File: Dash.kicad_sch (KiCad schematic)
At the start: 89 parts, among them J1 Conn_01x03_Socket, J10 Conn_01x03_Socket, J11 Conn_01x04_Socket, J2 Conn_01x03_Socket, J3 Conn_01x03_Socket, J4 Conn_01x03_Socket, J5 Conn_01x03_Socket, J6 Conn_01x03_Socket, J7 Conn_01x07_Socket, J8 Conn_01x06_Socket, J9 Conn_01x05_Socket, Q1 2N7000, Q16 NMOS, Q17 NMOS, Q18 NMOS, Q19 NMOS, Q2 NMOS, Q20 NMOS, Q4 NMOS, Q5 NMOS, SW1 SW_Push, U1 SFH617A-1, U2 24C02Cx-x-SN, U3 24C02Cx-x-SN, U4 LM2678T-3.3, U5 LM2678T-5.0, U6 ESP32-S2-DevKitM

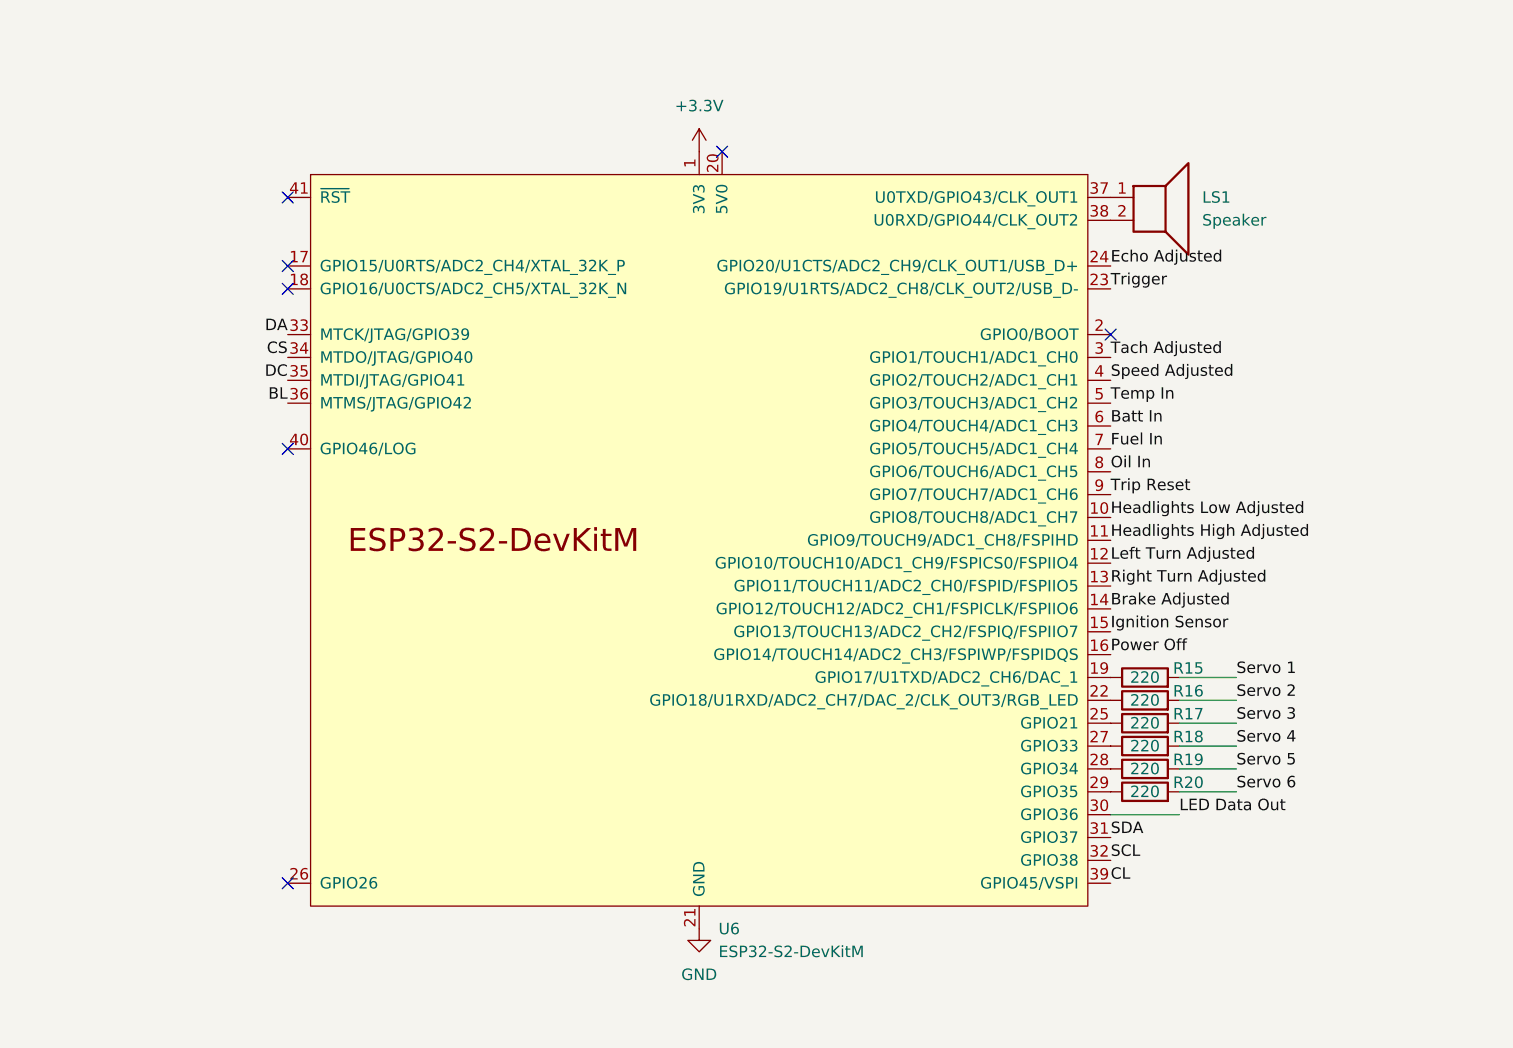
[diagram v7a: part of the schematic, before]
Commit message: Fixed pin assignments
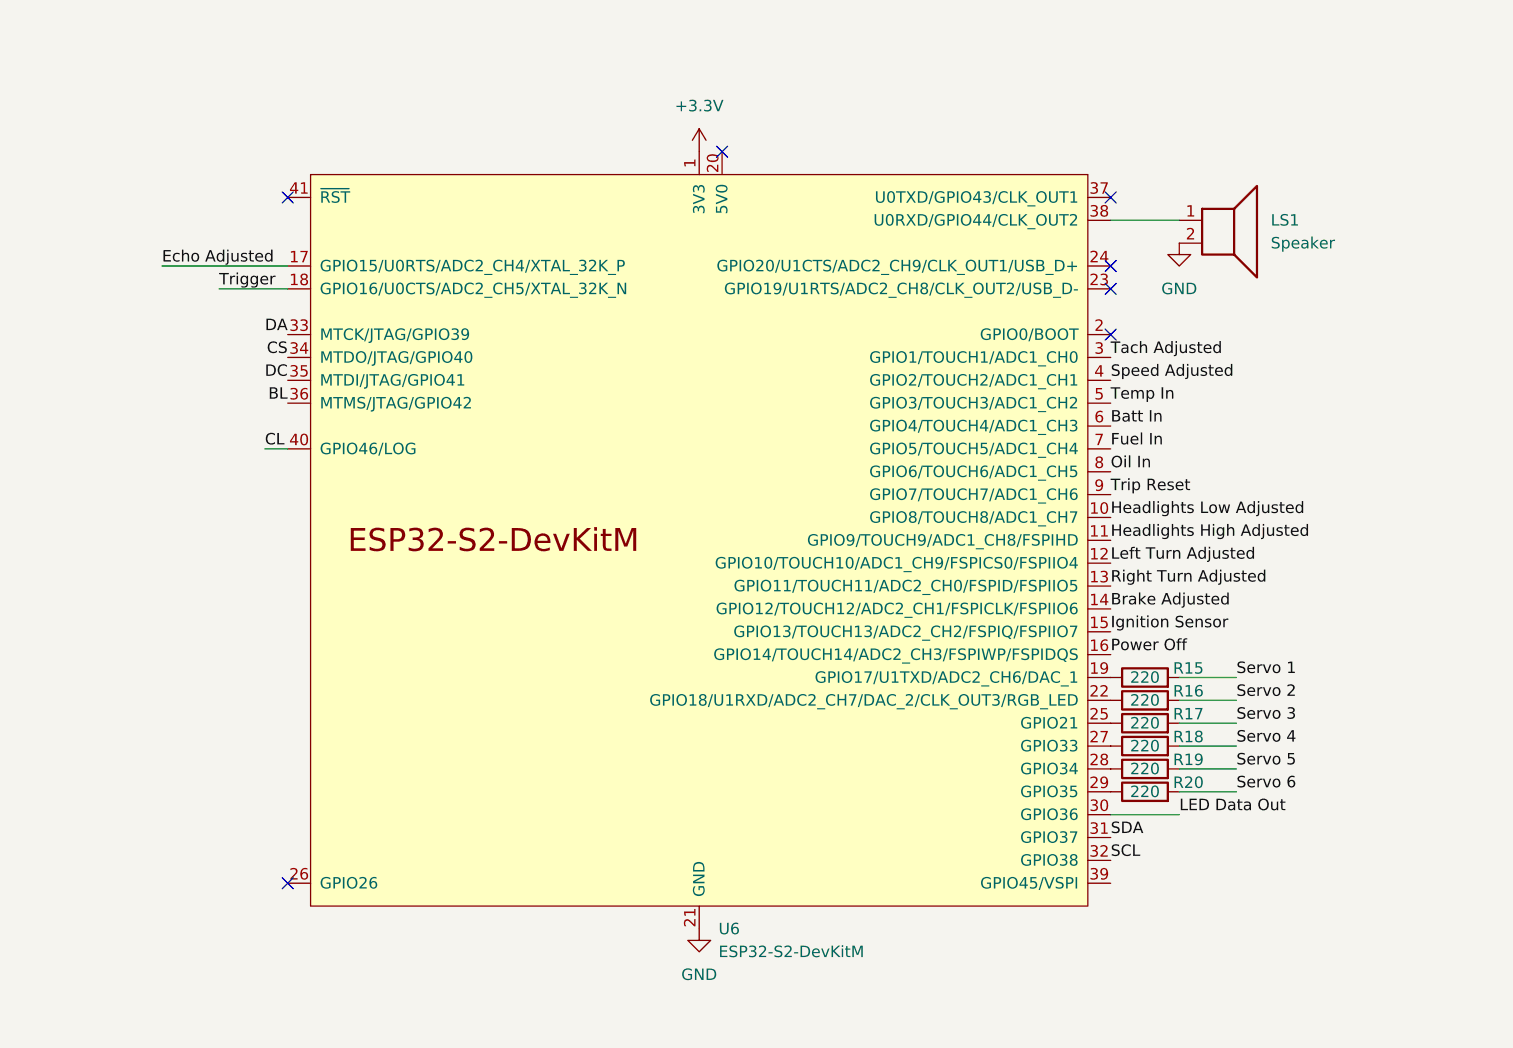
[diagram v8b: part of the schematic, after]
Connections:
- net CL: now also U6.40 (GPIO46/LOG); no longer U6.39 (GPIO45/VSPI)
- net Echo Adjusted: now also U6.17 (GPIO15/U0RTS/ADC2_CH4/XTAL_32K_P); no longer U6.24 (GPIO20/U1CTS/ADC2_CH9/CLK_OUT1/USB_D+)
- net GND: now also LS1.2
- net Trigger: now also U6.18 (GPIO16/U0CTS/ADC2_CH5/XTAL_32K_N); no longer U6.23 (GPIO19/U1RTS/ADC2_CH8/CLK_OUT2/USB_D-)
- net at U6.37 (U0TXD/GPIO43/CLK_OUT1): no longer LS1.1
- net at U6.38 (U0RXD/GPIO44/CLK_OUT2): now also LS1.1; no longer LS1.2
